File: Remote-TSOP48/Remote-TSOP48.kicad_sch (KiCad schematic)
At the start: 12 parts, among them J1 FFC-50, J6 SHIELD, U1 TSOP-48

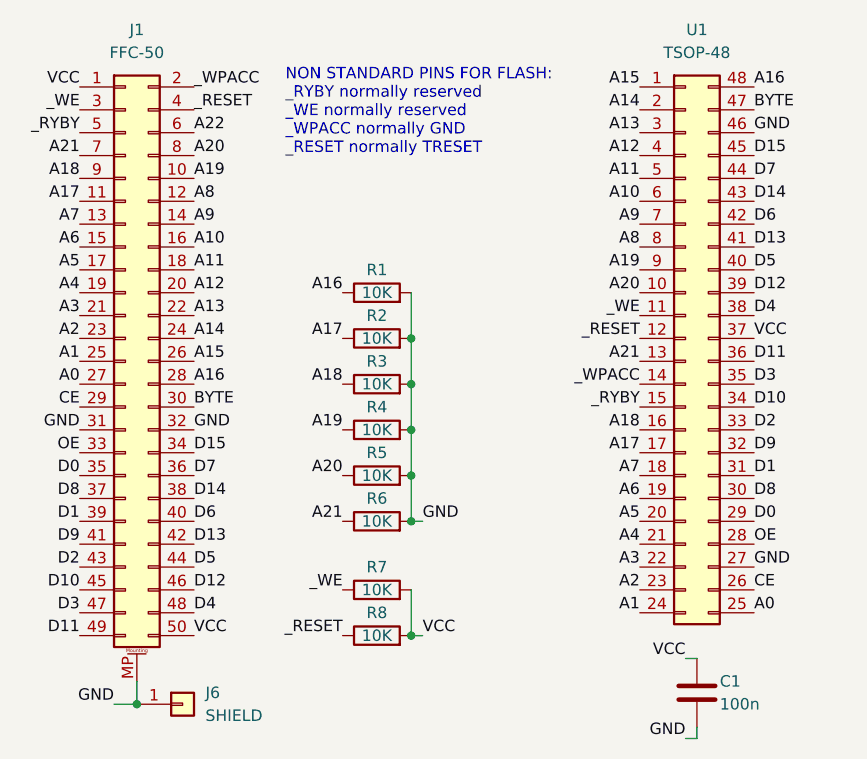
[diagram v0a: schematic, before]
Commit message: Remote-TSOP48 v1.1 accomodates 0603 or 0805 passives, connector moved down
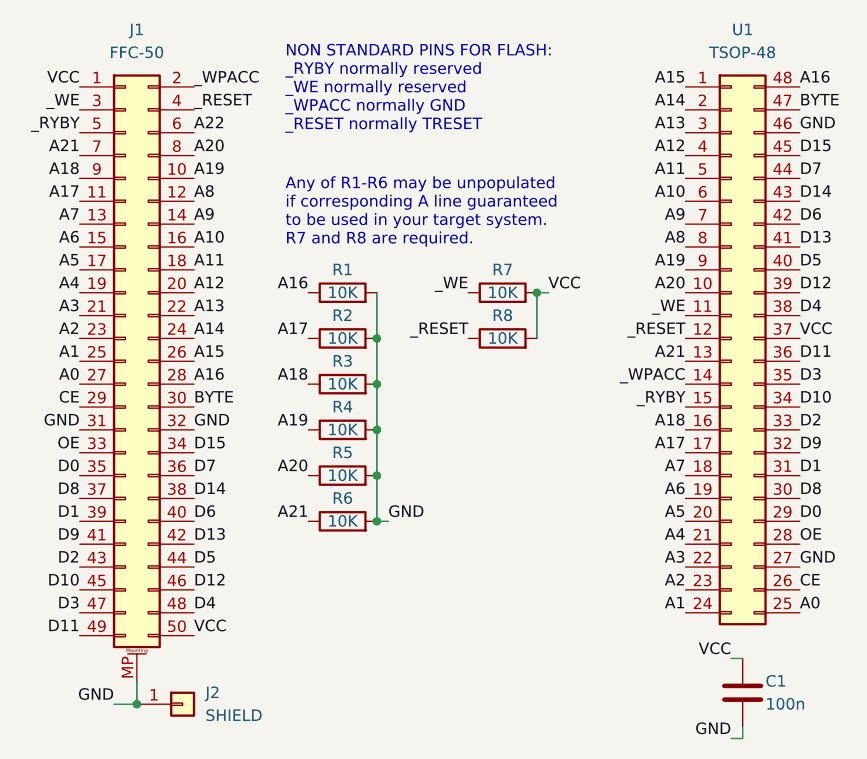
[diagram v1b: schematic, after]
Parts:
- C1: footprint Capacitor_SMD:C_0603_1608Metric -> Capacitor_SMD:C_0603_1608Metric_Pad1.08x0.95mm_HandSolder
- R1, R2, R3, R4, R5, R6, R7, R8: footprint Resistor_SMD:R_0603_1608Metric -> Resistor_SMD:R_0603_1608Metric_Pad0.98x0.95mm_HandSolder
- renumbered J6 to J2
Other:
- note added: "Any of R1-R6 may be unpopulated if corresponding A line guaranteed to be used in your target system. R7 and R8 are required."
- moved on the sheet: C1, R1, R2, R3, R4, R5, R6, R7, R8, U1
